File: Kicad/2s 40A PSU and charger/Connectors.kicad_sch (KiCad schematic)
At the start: 18 parts, among them J1 Keystone 3579, J10 G-Switch-GT-USB-7025, J11 1.27mm 4 pin socket, J2 JST XH-S Balance Plug, J3 Keystone 3579, J4 Keystone 3569, J5 Keystone 3569, J6 Keystone 3579, J7 Keystone 3579, J8 Keystone 3569, J9 Keystone 3569

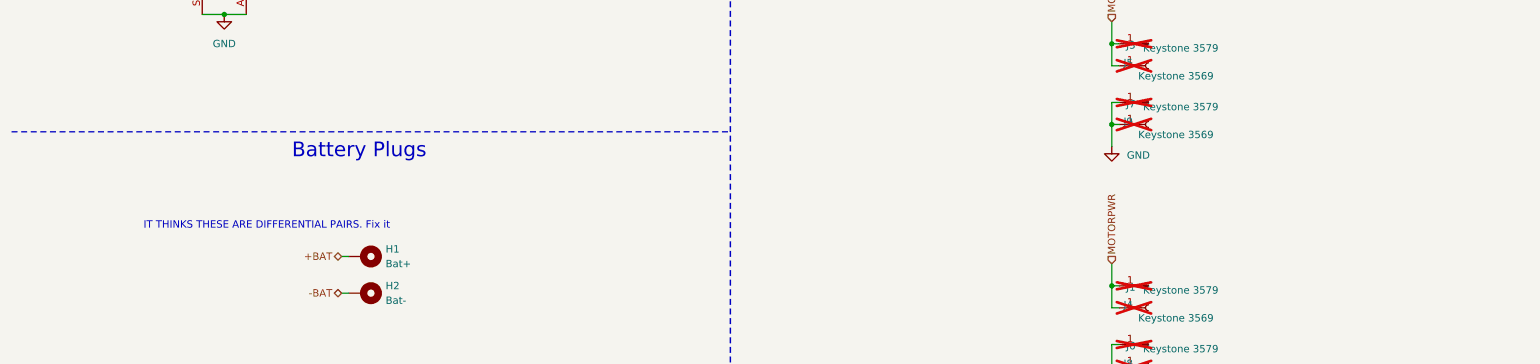
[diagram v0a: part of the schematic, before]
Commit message: Final tweaks, capacitor placement and GND keepouts
I tried my best to isolate signal grounds from the power paths. I also added a bunch of ground keepouts to help isolate.
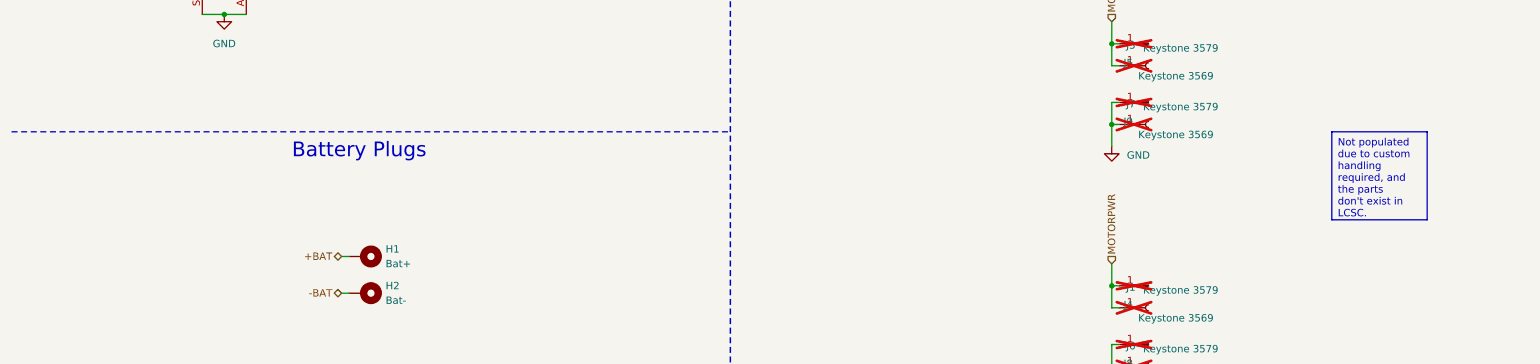
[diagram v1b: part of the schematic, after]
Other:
- note removed: "IT THINKS THESE ARE DIFFERENTIAL PAIRS. Fix it"
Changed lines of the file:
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@@
 	(title_block
 		(title "CACKLE 2s 40A PSU & Charger")
-		(date "2024-12-01")
+		(date "2024-12-23")
 		(rev "V1")
 		(comment 1 "Author: Asher Edwards")
@@
 		(at 87.63 77.47 0)
 		(size 11.43 7.62)
+		(stroke
+			(width 0)
+			(type default)
+		)
+		(fill
+			(type none)
+		)
+		(effects
+			(font
+				(size 1.27 1.27)
+			)
+			(justify left top)
+		)
+	)
+	(text_box "Not populated due to custom handling required, and the parts don't exist in LCSC."
+		(exclude_from_sim no)
+		(at 240.03 110.49 0)
+		(size 16.51 15.24)
 		(stroke
 			(width 0)
@@
 			)
 		)
-	)
-	(text "IT THINKS THESE ARE DIFFERENTIAL PAIRS. Fix it"
-		(exclude_from_sim no)
-		(at 55.626 126.746 0)
-		(effects
-			(font
-				(size 1.27 1.27)
-			)
-		)

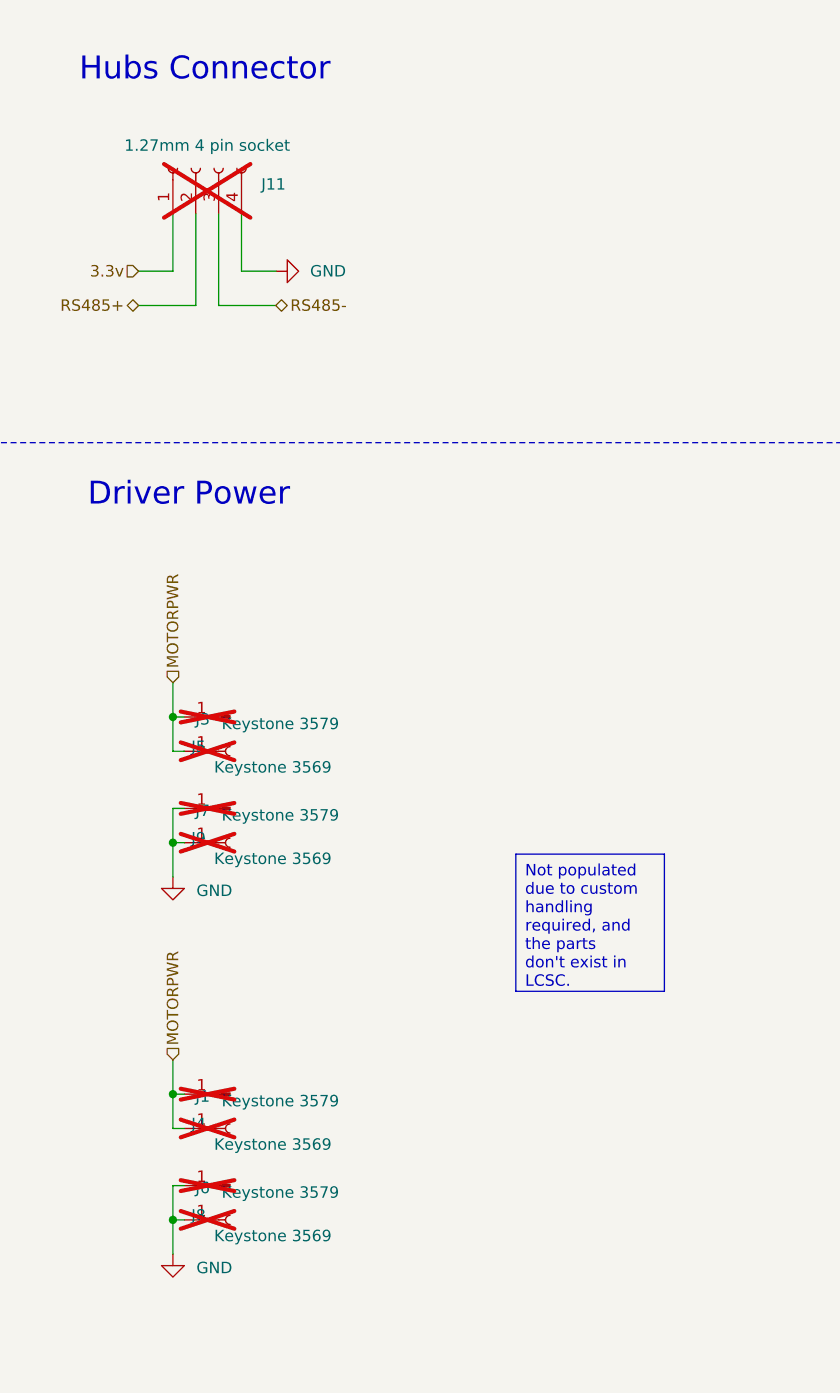
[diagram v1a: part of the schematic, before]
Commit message: Updated 3D models and usb length tuning for PSU
I also tweaked some of the USB length tuning to have the same length at EVERY stop, not just the end. So the through holes should have a matched usb output, and the chip should also have a match.
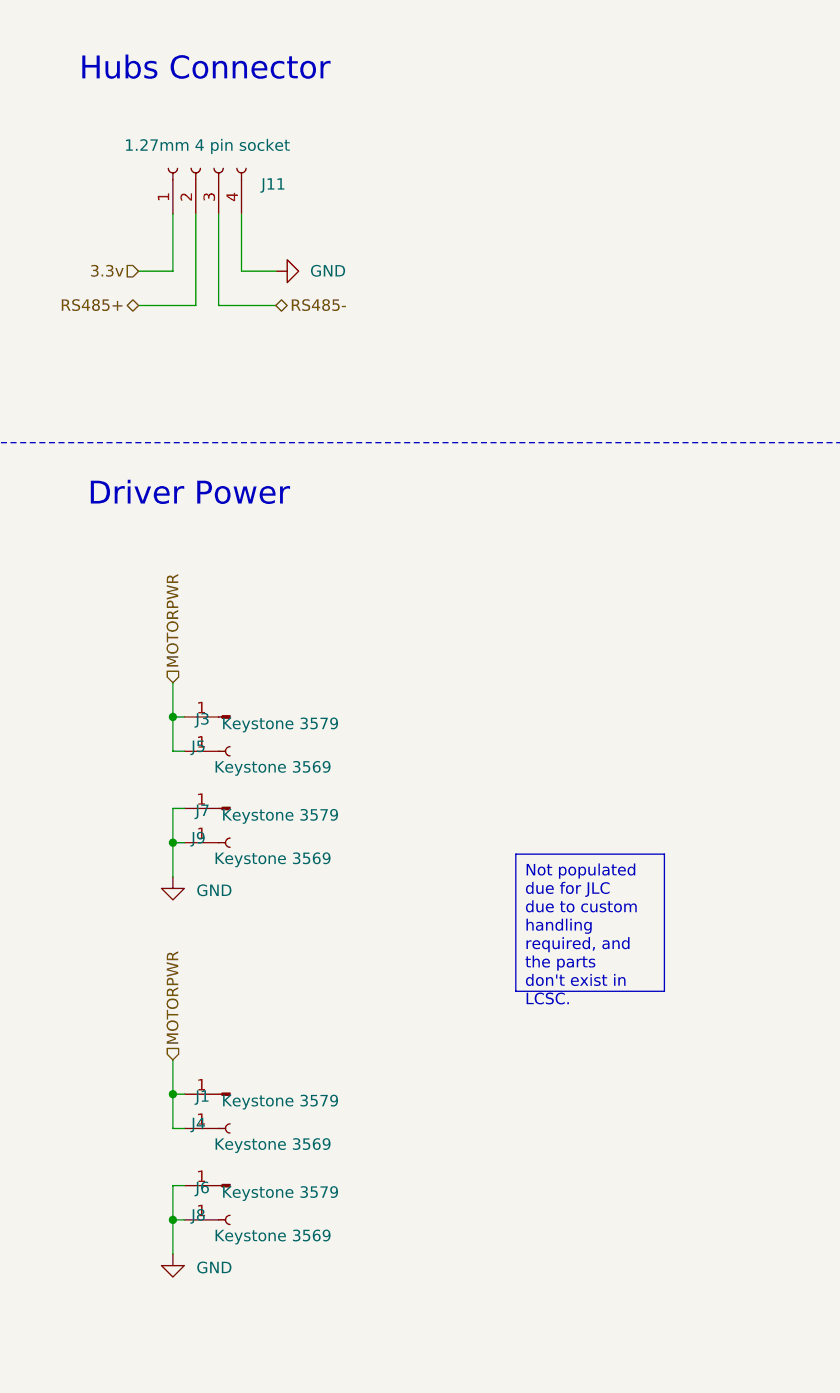
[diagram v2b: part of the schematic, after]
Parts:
- J1, J11, J3, J6, J7: now fitted
- J4, J5, J8, J9: footprint custom_Connector:Keystone_3569 -> custom_Connector:Keystone_3569_half; now fitted
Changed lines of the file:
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@@
 		)
 	)
-	(text_box "Not populated due to custom handling required, and the parts don't exist in LCSC."
+	(text_box "Not populated due for JLC due to custom handling required, and the parts don't exist in LCSC."
 		(exclude_from_sim no)
 		(at 240.03 110.49 0)
@@
 		(in_bom yes)
 		(on_board yes)
-		(dnp yes)
+		(dnp no)
 		(property "Reference" "J4"
 			(at 203.962 140.462 0)
@@
 			)
 		)
-		(property "Footprint" "custom_Connector:Keystone_3569"
+		(property "Footprint" "custom_Connector:Keystone_3569_half"
 			(at 208.28 140.97 0)
 			(effects
@@
 		(in_bom yes)
 		(on_board yes)
-		(dnp yes)
+		(dnp no)
 		(property "Reference" "J7"
 			(at 205.232 105.664 0)
@@
 		(in_bom yes)
 		(on_board yes)
-		(dnp yes)
+		(dnp no)
 		(property "Reference" "J3"
 			(at 205.232 95.504 0)
@@
 		(in_bom yes)
 		(on_board yes)
-		(dnp yes)
+		(dnp no)
 		(property "Reference" "J1"
 			(at 205.232 137.414 0)
@@
 		(in_bom yes)
 		(on_board yes)
-		(dnp yes)
+		(dnp no)
 		(property "Reference" "J8"
 			(at 203.962 150.622 0)
@@
 			)
 		)
-		(property "Footprint" "custom_Connector:Keystone_3569"
+		(property "Footprint" "custom_Connector:Keystone_3569_half"
 			(at 208.28 151.13 0)
 			(effects
@@
 		(in_bom yes)
 		(on_board yes)
-		(dnp yes)
+		(dnp no)
 		(property "Reference" "J5"
 			(at 203.962 98.552 0)
@@
 			)
 		)
-		(property "Footprint" "custom_Connector:Keystone_3569"
+		(property "Footprint" "custom_Connector:Keystone_3569_half"
 			(at 208.28 99.06 0)
 			(effects
@@
 		(in_bom yes)
 		(on_board yes)
-		(dnp yes)
+		(dnp no)
 		(property "Reference" "J9"
 			(at 203.962 108.712 0)
@@
 			)
 		)
-		(property "Footprint" "custom_Connector:Keystone_3569"
+		(property "Footprint" "custom_Connector:Keystone_3569_half"
 			(at 208.28 109.22 0)
 			(effects
@@
 		(in_bom yes)
 		(on_board yes)
-		(dnp yes)
+		(dnp no)
 		(property "Reference" "J6"
 			(at 205.232 147.574 0)
@@
 		(in_bom yes)
 		(on_board yes)
-		(dnp yes)
+		(dnp no)
 		(property "Reference" "J11"
 			(at 213.106 36.068 90)

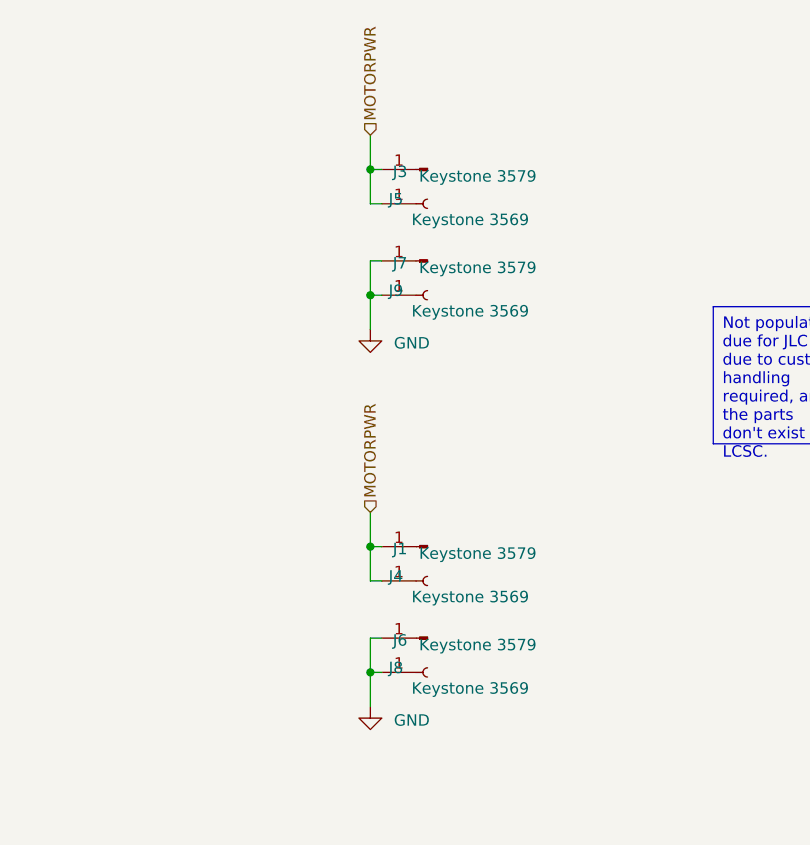
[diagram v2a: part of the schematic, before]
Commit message: Fixed 0.2mm offset in 3d model of Keystone 3579 connector
It was inset into the pcb a little which was causing some vertical misalignment in the CAD model. This affects nothing in real life, just a nice quality of life thing.
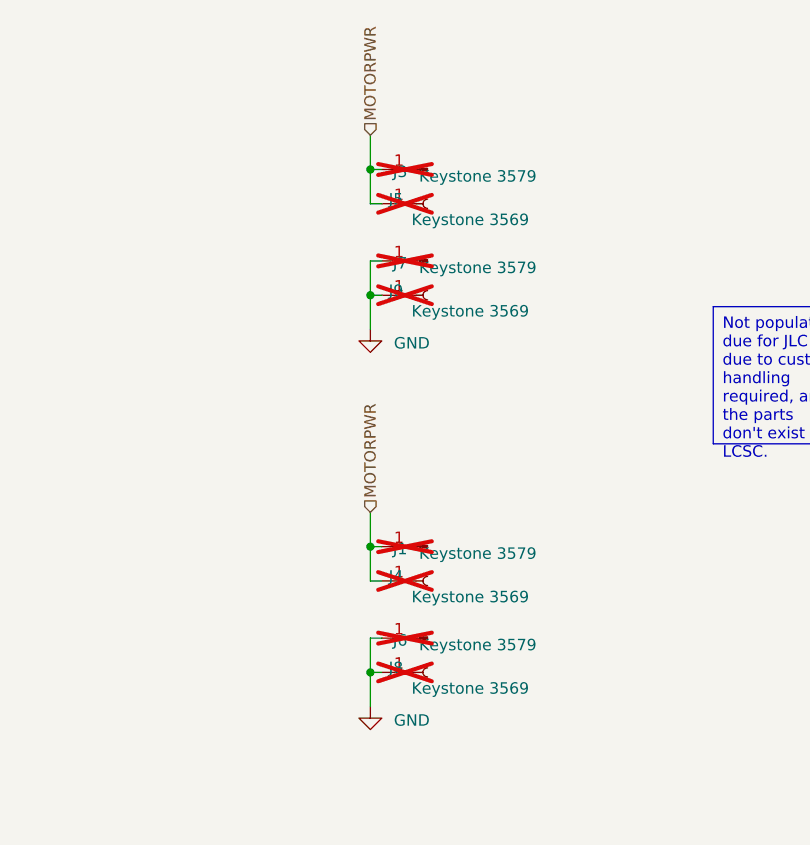
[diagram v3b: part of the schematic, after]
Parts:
- J1, J3, J4, J5, J6, J7, J8, J9: now not fitted
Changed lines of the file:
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@@
 		(in_bom yes)
 		(on_board yes)
-		(dnp no)
+		(dnp yes)
 		(property "Reference" "J4"
 			(at 203.962 140.462 0)
@@
 		(in_bom yes)
 		(on_board yes)
-		(dnp no)
+		(dnp yes)
 		(property "Reference" "J7"
 			(at 205.232 105.664 0)
@@
 		(in_bom yes)
 		(on_board yes)
-		(dnp no)
+		(dnp yes)
 		(property "Reference" "J3"
 			(at 205.232 95.504 0)
@@
 		(in_bom yes)
 		(on_board yes)
-		(dnp no)
+		(dnp yes)
 		(property "Reference" "J1"
 			(at 205.232 137.414 0)
@@
 		(in_bom yes)
 		(on_board yes)
-		(dnp no)
+		(dnp yes)
 		(property "Reference" "J8"
 			(at 203.962 150.622 0)
@@
 		(in_bom yes)
 		(on_board yes)
-		(dnp no)
+		(dnp yes)
 		(property "Reference" "J5"
 			(at 203.962 98.552 0)
@@
 		(in_bom yes)
 		(on_board yes)
-		(dnp no)
+		(dnp yes)
 		(property "Reference" "J9"
 			(at 203.962 108.712 0)
@@
 		(in_bom yes)
 		(on_board yes)
-		(dnp no)
+		(dnp yes)
 		(property "Reference" "J6"
 			(at 205.232 147.574 0)
